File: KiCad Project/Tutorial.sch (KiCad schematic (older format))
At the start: 26 parts, among them J1 USB_mini_micro_B, K1 KEYSW, K2 KEYSW, K3 KEYSW, K4 KEYSW, K5 KEYSW, SW1 SW_PUSH, U1 ATMEGA32U4, Y2 16Mhz

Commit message: Added fuse
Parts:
- added F1: 500mA, symbol Device:Polyfuse_Small
- added F?: Fuse, symbol Device:Fuse
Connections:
- net VCC: now also F1.2; no longer U1.2 (UVcc)
- new net: F1.1, U1.2 (UVcc)
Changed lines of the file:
@@
 Connection ~ 3000 2500
 Wire Wire Line
-	3000 2500 3950 2500
+	3000 2500 3450 2500
 $Comp
 L Device:R_Small R3
@@
 Wire Wire Line
 	2650 4200 2650 4400
+$Comp
+L Device:Fuse F?
+U 1 1 5EE94B86
+P 6700 3950
+F 0 "F?" H 6760 3996 50  0000 L CNN
+F 1 "Fuse" H 6760 3905 50  0000 L CNN
+F 2 "" V 6630 3950 50  0001 C CNN
+F 3 "~" H 6700 3950 50  0001 C CNN
+	1    6700 3950
+	1    0    0    -1
+$EndComp
+$Comp
+L Device:Polyfuse_Small F1
+U 1 1 5EE95BEE
+P 3550 2500
+F 0 "F1" V 3345 2500 50  0000 C CNN
+F 1 "500mA" V 3436 2500 50  0000 C CNN
+F 2 "" H 3600 2300 50  0001 L CNN
+F 3 "~" H 3550 2500 50  0001 C CNN
+	1    3550 2500
+	0    1    1    0
+$EndComp
+Wire Wire Line
+	3650 2500 3950 2500
 $EndSCHEMATC

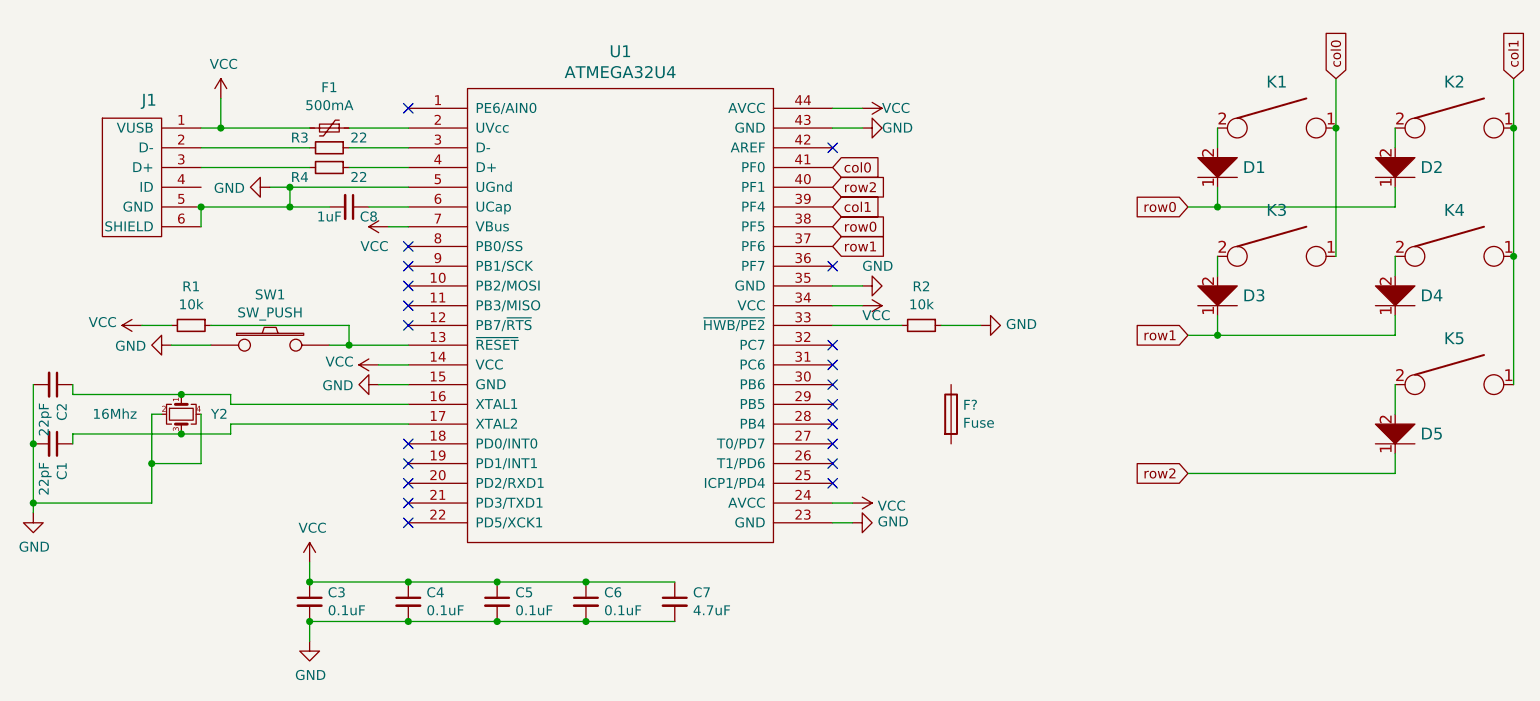
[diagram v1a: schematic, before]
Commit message: Added Fuse
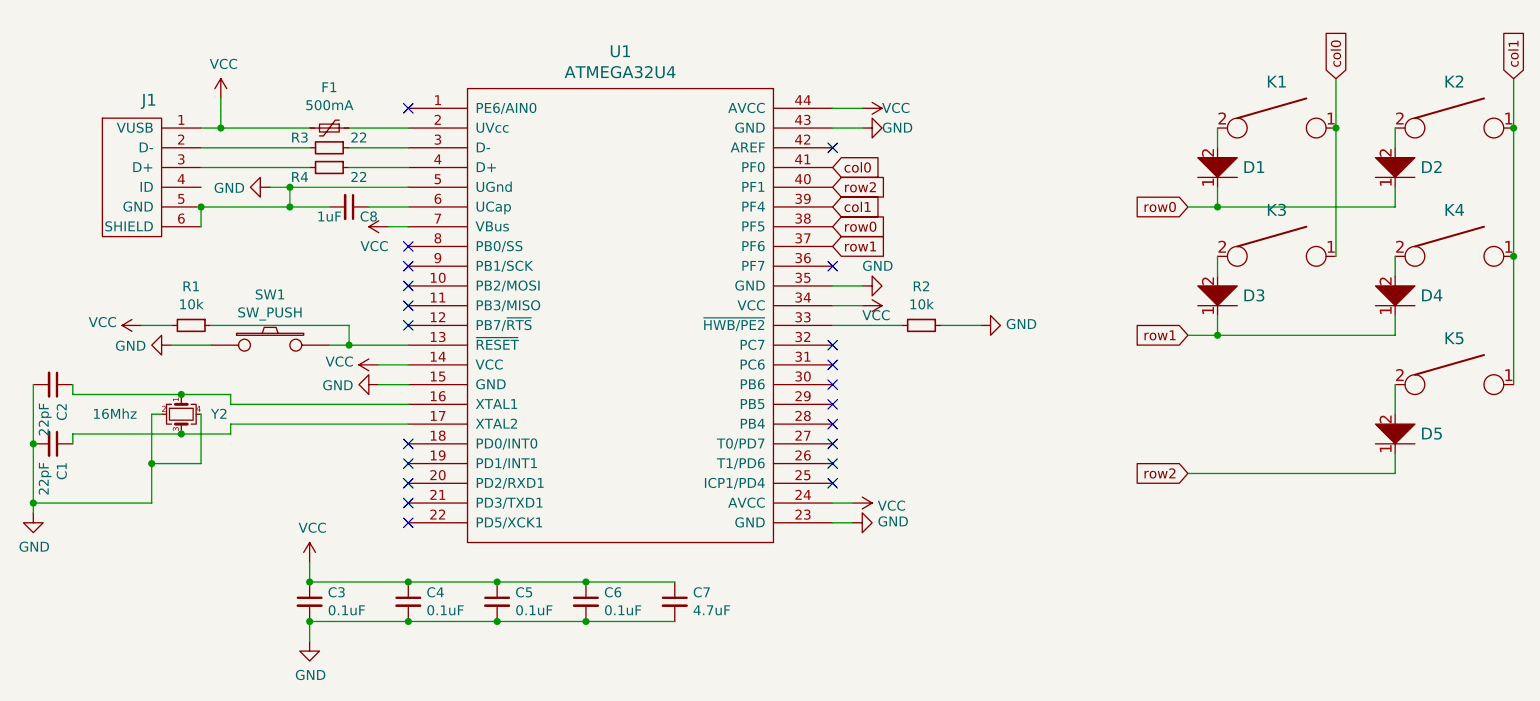
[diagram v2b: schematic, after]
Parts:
- removed F?: Fuse, symbol Device:Fuse
- F1: footprint (none) -> Fuse:Fuse_1206_3216Metric
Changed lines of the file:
@@
 Wire Wire Line
 	3000 2500 3000 2350
-Connection ~ 3000 2500
-Wire Wire Line
-	3000 2500 3450 2500
 $Comp
 L Device:R_Small R3
@@
 	2650 4200 2650 4400
 $Comp
-L Device:Fuse F?
-U 1 1 5EE94B86
-P 6700 3950
-F 0 "F?" H 6760 3996 50  0000 L CNN
-F 1 "Fuse" H 6760 3905 50  0000 L CNN
-F 2 "" V 6630 3950 50  0001 C CNN
-F 3 "~" H 6700 3950 50  0001 C CNN
-	1    6700 3950
-	1    0    0    -1
-$EndComp
-$Comp
 L Device:Polyfuse_Small F1
 U 1 1 5EE95BEE
@@
 F 0 "F1" V 3345 2500 50  0000 C CNN
 F 1 "500mA" V 3436 2500 50  0000 C CNN
-F 2 "" H 3600 2300 50  0001 L CNN
+F 2 "Fuse:Fuse_1206_3216Metric" H 3600 2300 50  0001 L CNN
 F 3 "~" H 3550 2500 50  0001 C CNN
 	1    3550 2500
@@
 Wire Wire Line
 	3650 2500 3950 2500
+Wire Wire Line
+	3450 2500 3000 2500
+Connection ~ 3000 2500
 $EndSCHEMATC
